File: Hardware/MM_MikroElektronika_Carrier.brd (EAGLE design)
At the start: 80 x 35.6 mm, 89 parts, among them J15 MICROMOD-2222-C, J2 QWIIC_RIGHT_ANGLE, J5 Vertical Qwiic Connector, U1 MCP73831, U5 AP7361C-33FGEUDFN-8

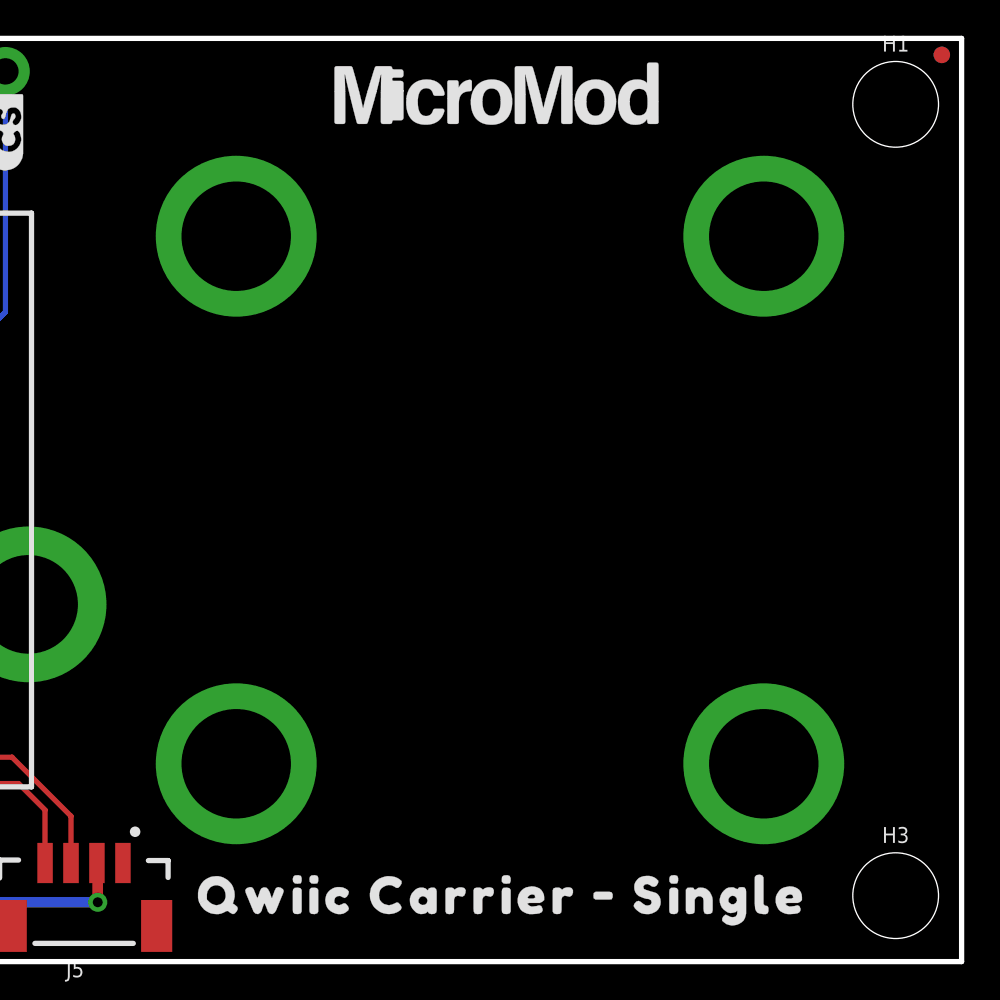
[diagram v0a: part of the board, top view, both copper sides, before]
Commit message: Renamed eagle files
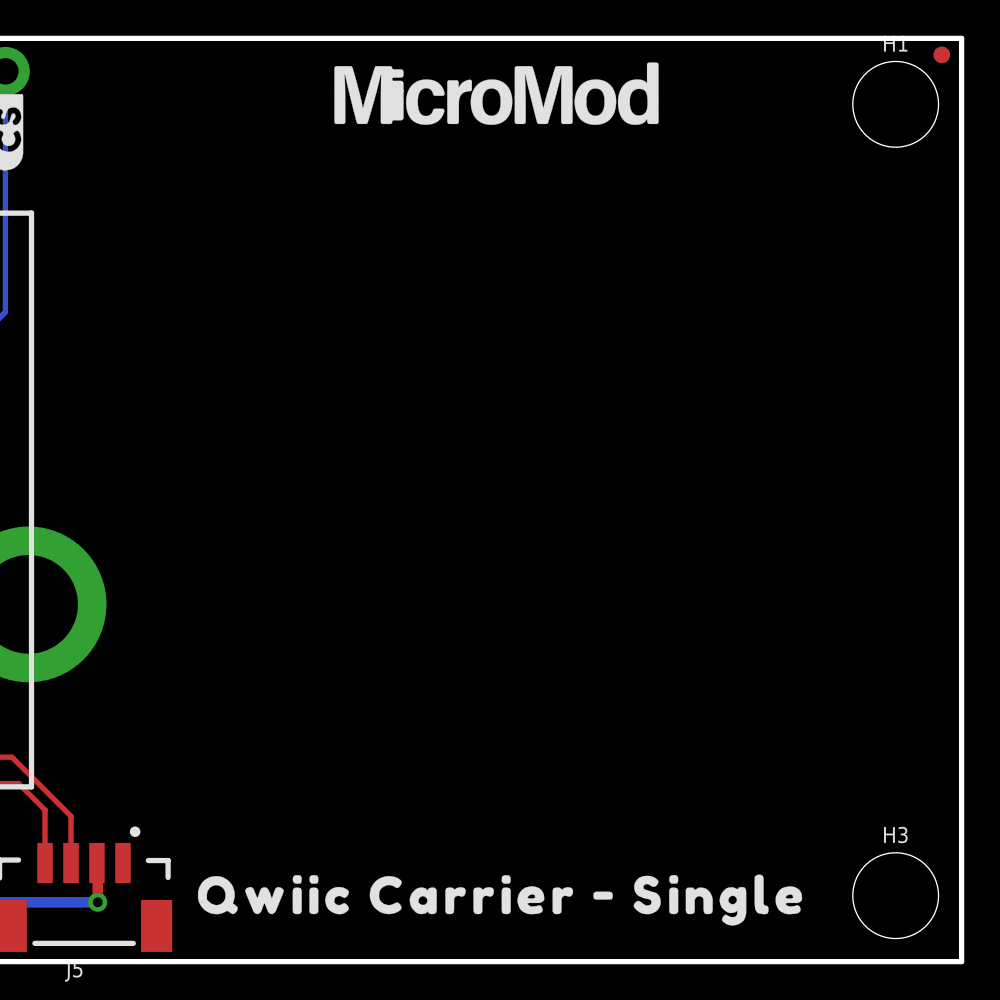
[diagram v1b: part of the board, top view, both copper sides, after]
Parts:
- removed U$5: QWIIC_BOARD_OUTLINESTANDOFF, SparkFun-Boards:QWIIC_BOARD_MOUNT_SMD_STANDOFFS
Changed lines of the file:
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@@
 <?xml version="1.0" encoding="utf-8"?>
 <!DOCTYPE eagle SYSTEM "eagle.dtd">
-<eagle version="9.5.2">
+<eagle version="9.4.2">
 <drawing>
 <settings>
@@
 <attribute name="VALUE" x="46.212" y="5.86833125" size="0.6096" layer="27" rot="R180"/>
 </element>
-<element name="U$5" library="SparkFun-Boards" package="QWIIC_BOARD_MOUNT_SMD_STANDOFFS" value="QWIIC_BOARD_OUTLINESTANDOFF" x="62.23" y="17.78" smashed="yes"/>
 <element name="U$3" library="output" package="3V30" value="" x="5.715" y="33.655" smashed="yes"/>
 <element name="U$1" library="output" package="#3#3V_EN#0" value="" x="15.748" y="16.51" smashed="yes" rot="MR0"/>
